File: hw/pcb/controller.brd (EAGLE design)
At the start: 76.2 x 50.5 mm, 26 parts, among them IC1 MCP23017SS, Q1 MOSFET-NCH, U2 TMP102, U3 MCP6004, U4 MCP2510SO

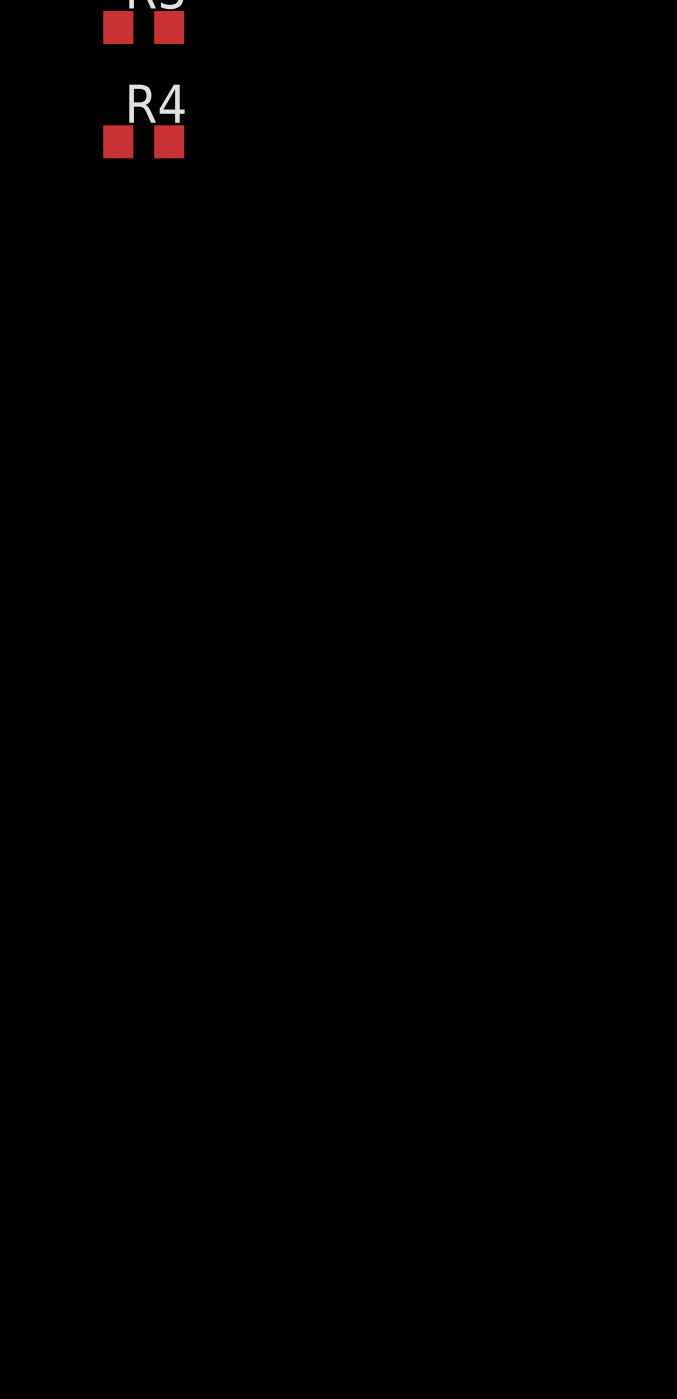
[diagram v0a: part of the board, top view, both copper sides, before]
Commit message: working aux control over mqtt; working multi-input and inversion
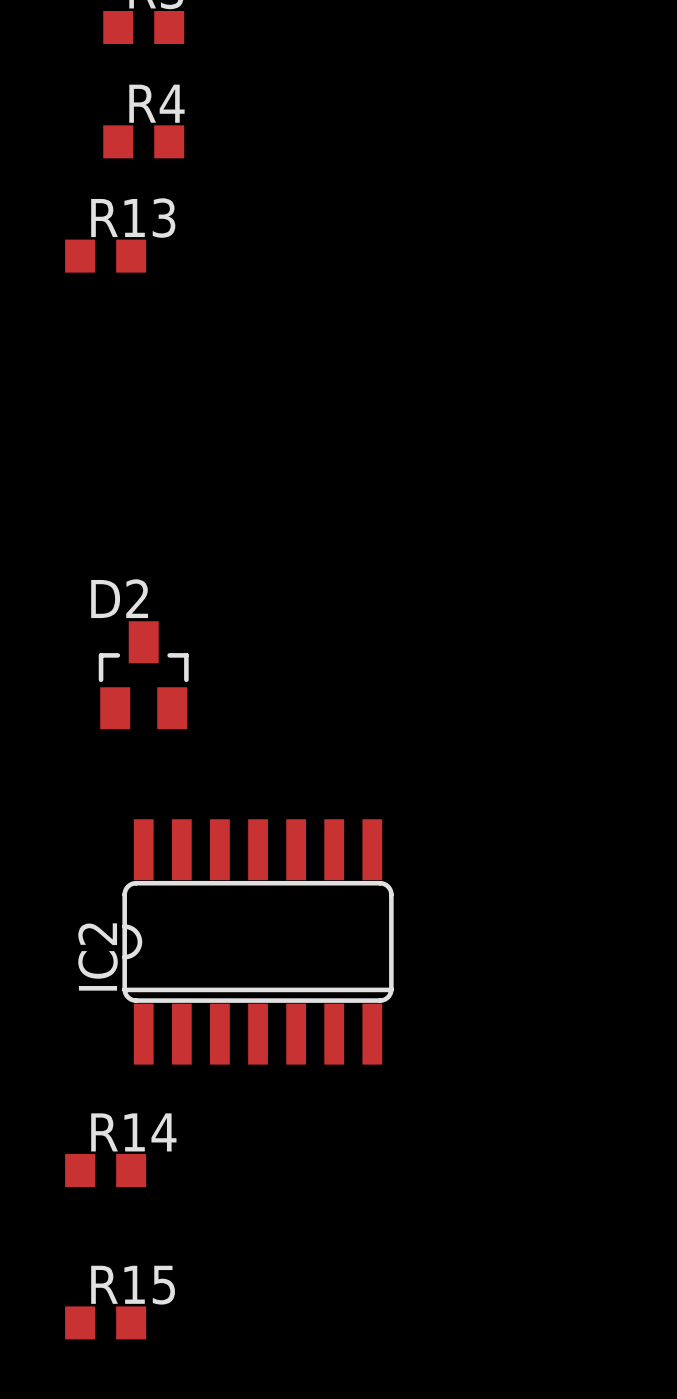
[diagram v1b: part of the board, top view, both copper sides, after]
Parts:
- added D2: MMBZ, curtek:SOT23
- added IC2: 4001D, 40xx:SO14
- added R13: 10k, rcl:R0603
- added R14, R15: 56k, rcl:R0603
- R10: value 10k -> 100k
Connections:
- new net INPUT_1: R13.2, X5.P$1
- new net INPUT_2: X5.P$2
- new net INPUT_3: X5.P$3
- new net INPUT_4: X5.P$4
- new net INPUT_5: X5.P$5
- new net INPUT_6: X5.P$6
- new net INPUT_7: X5.P$7
- new net INPUT_8: X5.P$8
- new net N$13: IC2.3, IC2.5
- new net N$15: IC2.1, R14.1
- new net N$16: IC2.6, R15.1
- new net N$17: IC2.2, IC2.4
- new net N$21: X5.P$9
- new net N$22: X5.P$10
- new net N$23: X5.P$11
- new net N$24: X5.P$12
- new net N$9: D2.1
- net GND: now also D2.3, R14.2, R15.2
- net INPUT_ACCESSORY: now also D2.2, R13.1
- net VDD: now also IC2.14
- net VSS: now also IC2.7
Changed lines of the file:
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@@
 <element name="R9" library="rcl" package="R0603" value="" x="-13.97" y="27.94"/>
 <element name="C1" library="rcl" package="C0603K" value="0.1uF" x="-13.97" y="24.13"/>
-<element name="R10" library="rcl" package="R0603" value="10k" x="-13.97" y="19.05"/>
+<element name="R10" library="rcl" package="R0603" value="100k" x="-13.97" y="19.05"/>
 <element name="Q1" library="SparkFun-DiscreteSemi" package="SOT23-3" value="MOSFET-NCH" x="-17.78" y="19.05">
 <attribute name="PROD_ID" value="TRAN-12988" x="-17.78" y="19.05" size="1.778" layer="27" display="off"/>
@@
 <attribute name="NAME" x="48.26" y="34.5821" size="1.778" layer="25" ratio="10" rot="R180"/>
 </element>
+<element name="R13" library="rcl" package="R0603" value="10k" x="-17.78" y="-17.78"/>
+<element name="D2" library="curtek" package="SOT23" value="MMBZ" x="-16.51" y="-31.75"/>
+<element name="IC2" library="40xx" package="SO14" value="4001D" x="-12.7" y="-40.64"/>
+<element name="R14" library="rcl" package="R0603" value="56k" x="-17.78" y="-48.26"/>
+<element name="R15" library="rcl" package="R0603" value="56k" x="-17.78" y="-53.34"/>
 </elements>
 <signals>
@@
 <contactref element="X6" pad="P$1"/>
 <contactref element="X2" pad="P$1"/>
-<wire x1="-16.93" y1="8.89" x2="-16.93" y2="3.81" width="0" layer="19" extent="1-1"/>
+<contactref element="D2" pad="3"/>
+<contactref element="R15" pad="2"/>
+<contactref element="R14" pad="2"/>
+<wire x1="51.215" y1="30.295" x2="72.39" y2="41.91" width="0" layer="19" extent="1-1"/>
+<wire x1="50.565" y1="30.295" x2="51.215" y2="30.295" width="0" layer="19" extent="1-1"/>
+<wire x1="49.915" y1="30.295" x2="50.565" y2="30.295" width="0" layer="19" extent="1-1"/>
+<wire x1="48.615" y1="23.045" x2="49.915" y2="30.295" width="0" layer="19" extent="1-1"/>
+<wire x1="28.8322" y1="24.13" x2="48.615" y2="23.045" width="0" layer="19" extent="1-1"/>
+<wire x1="20.55" y1="6.86" x2="28.8322" y2="24.13" width="0" layer="19" extent="1-1"/>
+<wire x1="9.12" y1="6.86" x2="20.55" y2="6.86" width="0" layer="19" extent="1-1"/>
+<wire x1="62.69" y1="6.86" x2="48.615" y2="23.045" width="0" layer="19" extent="1-1"/>
+<wire x1="-16.93" y1="8.89" x2="9.12" y2="6.86" width="0" layer="19" extent="1-1"/>
+<wire x1="-16.93" y1="3.81" x2="-16.93" y2="8.89" width="0" layer="19" extent="1-1"/>
 <wire x1="-16.83" y1="18.05" x2="-16.93" y2="8.89" width="0" layer="19" extent="1-1"/>
 <wire x1="-14.82" y1="19.05" x2="-16.83" y2="18.05" width="0" layer="19" extent="1-1"/>
 <wire x1="-13.095" y1="24.13" x2="-14.82" y2="19.05" width="0" layer="19" extent="1-1"/>
-<wire x1="28.8322" y1="24.13" x2="-13.095" y2="24.13" width="0" layer="19" extent="1-1"/>
-<wire x1="-14.82" y1="46.99" x2="28.8322" y2="24.13" width="0" layer="19" extent="1-1"/>
-<wire x1="48.615" y1="23.045" x2="-14.82" y2="46.99" width="0" layer="19" extent="1-1"/>
-<wire x1="49.915" y1="30.295" x2="48.615" y2="23.045" width="0" layer="19" extent="1-1"/>
-<wire x1="50.565" y1="30.295" x2="49.915" y2="30.295" width="0" layer="19" extent="1-1"/>
-<wire x1="51.215" y1="30.295" x2="50.565" y2="30.295" width="0" layer="19" extent="1-1"/>
-<wire x1="-13.47" y1="66.7" x2="49.915" y2="30.295" width="0" layer="19" extent="1-1"/>
-<wire x1="-13.97" y1="65.38" x2="-13.47" y2="66.7" width="0" layer="19" extent="1-1"/>
+<wire x1="-17.36" y1="-10.16" x2="-16.93" y2="3.81" width="0" layer="19" extent="1-1"/>
+<wire x1="-16.51" y1="-30.65" x2="-17.36" y2="-10.16" width="0" layer="19" extent="1-1"/>
+<wire x1="-16.93" y1="-48.26" x2="-16.51" y2="-30.65" width="0" layer="19" extent="1-1"/>
+<wire x1="-16.93" y1="-53.34" x2="-16.93" y2="-48.26" width="0" layer="19" extent="1-1"/>
+<wire x1="-14.82" y1="46.99" x2="-13.095" y2="24.13" width="0" layer="19" extent="1-1"/>
+<wire x1="-13.97" y1="65.38" x2="-14.82" y2="46.99" width="0" layer="19" extent="1-1"/>
+<wire x1="-13.47" y1="66.7" x2="-13.97" y2="65.38" width="0" layer="19" extent="1-1"/>
 <wire x1="-13.97" y1="68.5499" x2="-13.47" y2="66.7" width="0" layer="19" extent="1-1"/>
-<wire x1="9.12" y1="6.86" x2="51.215" y2="30.295" width="0" layer="19" extent="1-1"/>
-<wire x1="20.55" y1="6.86" x2="9.12" y2="6.86" width="0" layer="19" extent="1-1"/>
-<wire x1="-17.36" y1="-10.16" x2="20.55" y2="6.86" width="0" layer="19" extent="1-1"/>
-<wire x1="3.93" y1="45.06" x2="-17.36" y2="-10.16" width="0" layer="19" extent="1-1"/>
-<wire x1="62.69" y1="6.86" x2="-17.36" y2="-10.16" width="0" layer="19" extent="1-1"/>
-<wire x1="72.39" y1="41.91" x2="62.69" y2="6.86" width="0" layer="19" extent="1-1"/>
+<wire x1="3.93" y1="45.06" x2="-14.82" y2="46.99" width="0" layer="19" extent="1-1"/>
 </signal>
 <signal name="ESP_SCL">
@@
 <contactref element="R10" pad="2"/>
 <contactref element="Q1" pad="1"/>
-<wire x1="-13.12" y1="19.05" x2="-18.73" y2="18.05" width="0" layer="19" extent="1-1"/>
-<wire x1="56.69" y1="6.86" x2="-13.12" y2="19.05" width="0" layer="19" extent="1-1"/>
+<contactref element="R13" pad="1"/>
+<contactref element="D2" pad="2"/>
+<wire x1="-13.12" y1="19.05" x2="56.69" y2="6.86" width="0" layer="19" extent="1-1"/>
+<wire x1="-18.73" y1="18.05" x2="-13.12" y2="19.05" width="0" layer="19" extent="1-1"/>
+<wire x1="-18.63" y1="-17.78" x2="-18.73" y2="18.05" width="0" layer="19" extent="1-1"/>
+<wire x1="-15.56" y1="-32.85" x2="-18.63" y2="-17.78" width="0" layer="19" extent="1-1"/>
 </signal>
 <signal name="N$1">
@@
 <signal name="VSS">
 <contactref element="U4" pad="9"/>
+<contactref element="IC2" pad="7"/>
+<wire x1="-8.89" y1="-43.7134" x2="49.2379" y2="45.72" width="0" layer="19" extent="1-1"/>
 </signal>
 <signal name="VDD">
 <contactref element="U4" pad="18"/>
+<contactref element="IC2" pad="14"/>
+<wire x1="-16.51" y1="-37.5666" x2="39.6621" y2="35.56" width="0" layer="19" extent="1-1"/>
+</signal>
+<signal name="N$9">
+<contactref element="D2" pad="1"/>
+</signal>
+<signal name="INPUT_1">
+<contactref element="R13" pad="2"/>
+<contactref element="X5" pad="P$1"/>
+<wire x1="-16.93" y1="-17.78" x2="44.33" y2="6.86" width="0" layer="19" extent="1-1"/>
+</signal>
+<signal name="INPUT_2">
+<contactref element="X5" pad="P$2"/>
+</signal>
+<signal name="INPUT_3">
+<contactref element="X5" pad="P$3"/>
+</signal>
+<signal name="INPUT_4">
+<contactref element="X5" pad="P$4"/>
+</signal>
+<signal name="INPUT_5">
+<contactref element="X5" pad="P$5"/>
+</signal>
+<signal name="INPUT_6">
+<contactref element="X5" pad="P$6"/>
+</signal>
+<signal name="INPUT_7">
+<contactref element="X5" pad="P$7"/>
+</signal>
+<signal name="INPUT_8">
+<contactref element="X5" pad="P$8"/>
+</signal>
+<signal name="N$21">
+<contactref element="X5" pad="P$9"/>
+</signal>
+<signal name="N$22">
+<contactref element="X5" pad="P$10"/>
+</signal>
+<signal name="N$23">
+<contactref element="X5" pad="P$11"/>
+</signal>
+<signal name="N$24">
+<contactref element="X5" pad="P$12"/>
+</signal>
+<signal name="N$13">
+<contactref element="IC2" pad="5"/>
+<contactref element="IC2" pad="3"/>
+<wire x1="-11.43" y1="-43.7134" x2="-13.97" y2="-43.7134" width="0" layer="19" extent="1-1"/>
+</signal>
+<signal name="N$15">
+<contactref element="IC2" pad="1"/>
+<contactref element="R14" pad="1"/>
+<wire x1="-16.51" y1="-43.7134" x2="-18.63" y2="-48.26" width="0" layer="19" extent="1-1"/>
+</signal>
+<signal name="N$16">
+<contactref element="IC2" pad="6"/>
+<contactref element="R15" pad="1"/>
+<wire x1="-10.16" y1="-43.7134" x2="-18.63" y2="-53.34" width="0" layer="19" extent="1-1"/>
+</signal>
+<signal name="N$17">
+<contactref element="IC2" pad="4"/>
+<contactref element="IC2" pad="2"/>
+<wire x1="-12.7" y1="-43.7134" x2="-15.24" y2="-43.7134" width="0" layer="19" extent="1-1"/>
 </signal>
 </signals>
